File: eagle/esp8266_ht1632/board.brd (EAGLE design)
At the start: 37.5 x 26 mm, 11 parts, among them IC1 LM1117MP-3.3

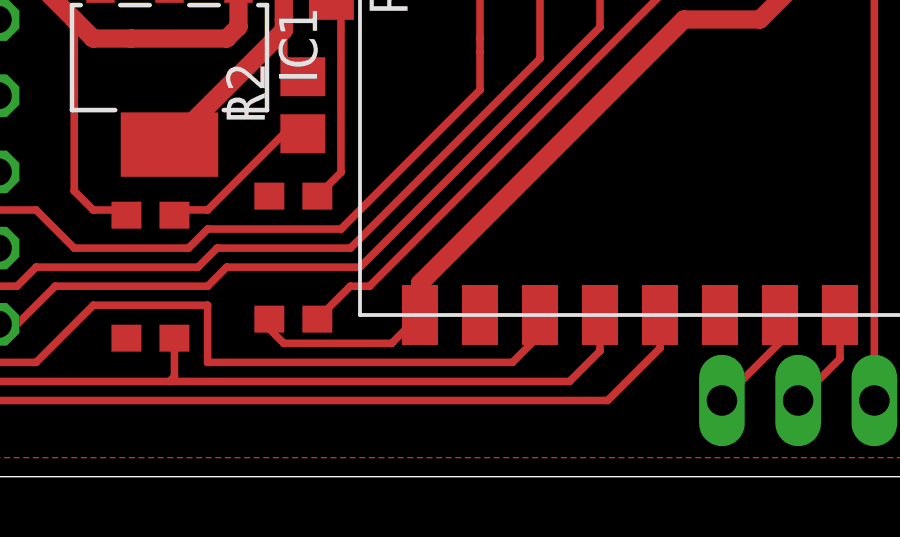
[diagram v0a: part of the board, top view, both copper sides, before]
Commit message: GPIO15 to GND to allow bootloading /bin/bash: q: command not found
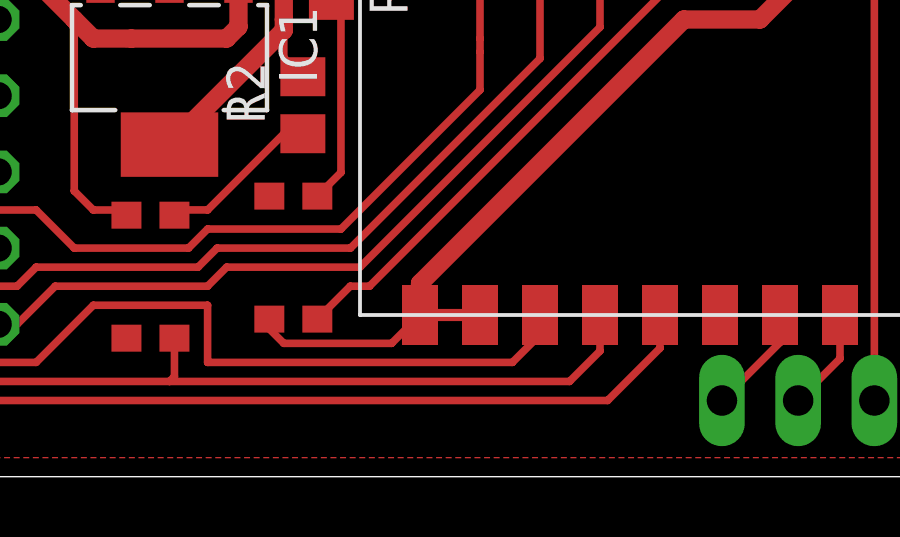
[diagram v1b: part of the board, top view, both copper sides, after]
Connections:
- net GND: now also U$1.2
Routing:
- net GND: track 110.9 -> 112.9 mm
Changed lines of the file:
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@@
 <wire x1="19.47" y1="4.445" x2="20.415" y2="5.39" width="0.254" layer="1"/>
 <wire x1="15.875" y1="4.445" x2="19.47" y2="4.445" width="0.254" layer="1"/>
+<contactref element="U$1" pad="2"/>
+<wire x1="22.415" y1="5.39" x2="20.415" y2="5.39" width="0.4064" layer="1"/>
 <wire x1="15.3925" y1="5.2525" x2="15.3925" y2="9.3525" width="0" layer="19" extent="1-1"/>
 <wire x1="10.63" y1="4.6175" x2="10.63" y2="8.7175" width="0" layer="19" extent="1-1"/>
